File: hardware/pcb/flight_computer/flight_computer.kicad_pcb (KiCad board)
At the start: 4 copper layers, 64 x 64 mm, 96 parts, among them J1 NRF24L01, J2 BATT_TERMINAL, J3 5V Terminal, J4 Pyro 1, J5 Pyro 2, J6 Servo, J7 Servo, J8 Conn_01x02, J9 Aux Ports, Q1 AO3401A, Q2 AO3401A, Q3 2N7002, Q4 AO3400A, Q5 2N7002, Q6 AO3401A, Q7 AO3400A, U2 TPS563201DDCR, U3 TPS73633DRBR, U4 BMP388, U5 LSM6DSRXTR, U6 Teensy4.1, U7 AZ1117-5.0

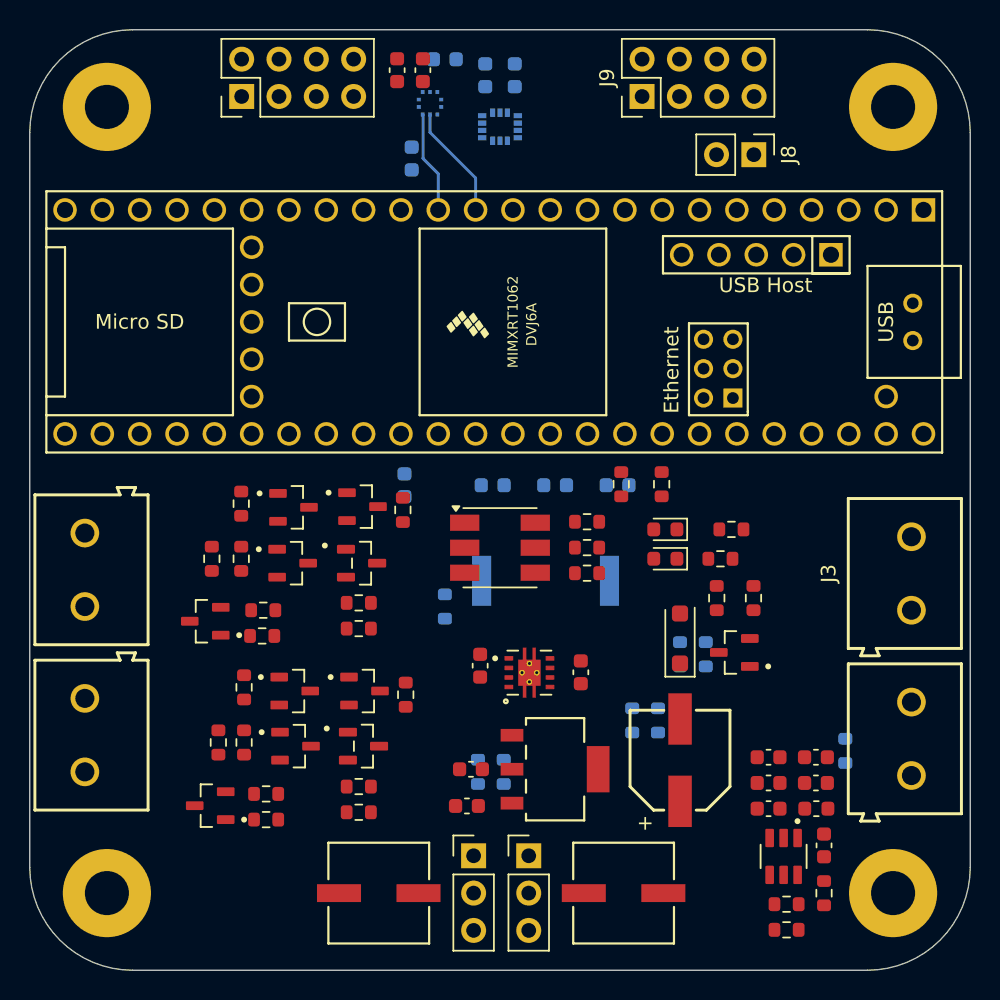
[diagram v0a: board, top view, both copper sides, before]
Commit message: Consolidate simulation and hardware into single ember repo
Absorb the standalone simulation repo into ember as plain files,
add root .gitignore, and update hardware CAD assets.

Co-Authored-By: Claude Opus 4.8 <noreply@anthropic.com>
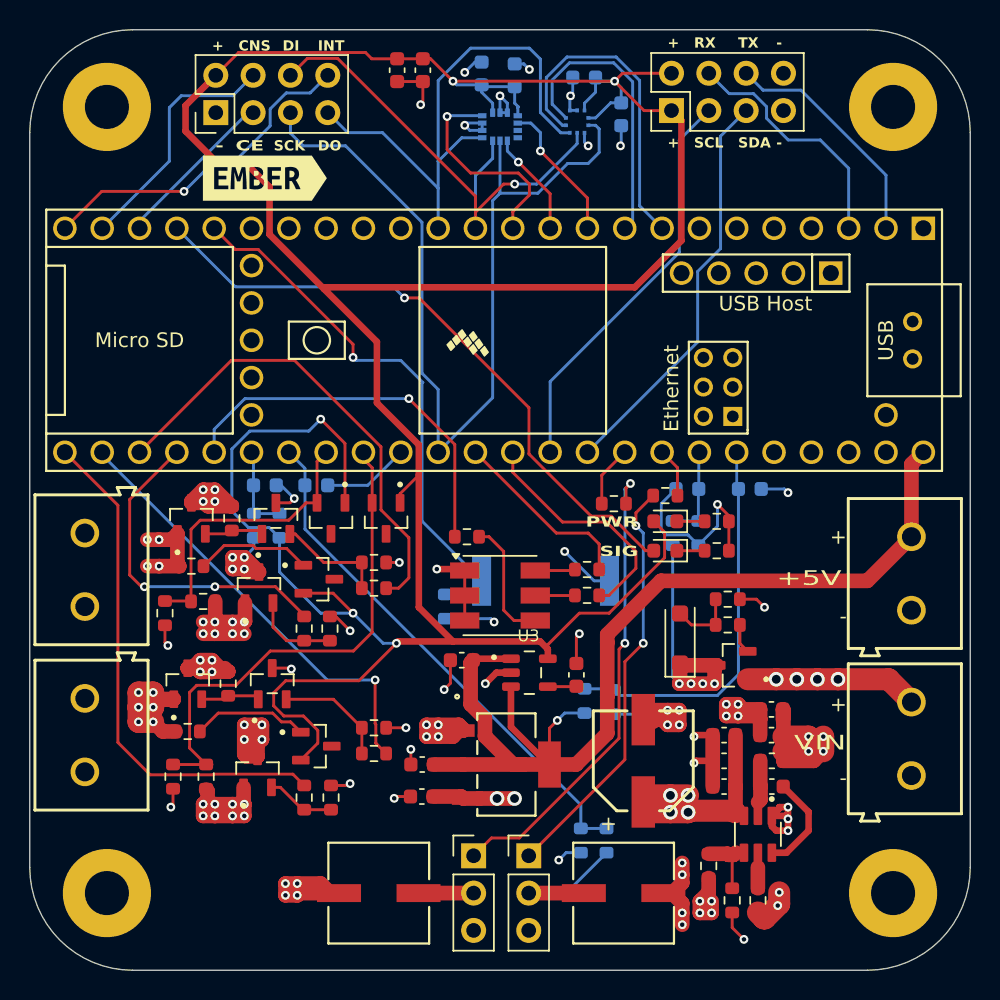
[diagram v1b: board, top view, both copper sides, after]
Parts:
- removed J8: Conn_01x02, Connector_PinHeader_2.54mm:PinHeader_1x02_P2.54mm_Vertical
- added kibuzzard-6A2E09AC: G***, kibuzzard-6A2E09AC, F.Cu at (134.0, 65.6)
- U3: footprint footprints:IC_DRV8601DRBT -> footprints:SOT95P280X145-5N
- moved R18 30.3 mm to (135.0, 89.2)
- moved R19 30.3 mm to (133.2, 89.2)
- moved C19 24.0 mm to (134.0, 86.5)
- moved D3 22.9 mm to (142.2, 88.8), turned to -90 degrees
- moved R17 16.1 mm to (157.8, 101.2)
- moved C4 14.6 mm to (158.2, 61.2)
- moved R7 13.5 mm to (163.5, 89.8)
- moved C12 13.3 mm to (162.8, 86.8)
- moved C18 13.3 mm to (167.0, 86.8)
- moved R6 12.8 mm to (161.8, 89.8)
- moved R8 12.1 mm to (131.5, 100.0), turned to -90 degrees
- moved Q2 12.0 mm to (128.8, 100.0), turned to 90 degrees
- moved Q6 11.7 mm to (129.0, 88.8), turned to 90 degrees
- moved R23 11.7 mm to (131.8, 88.8)
- moved D5 11.1 mm to (138.5, 88.8), turned to -90 degrees
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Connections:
- J1 pad 2: /CE_NRF -> +3.3V
- J1 pad 3: /Barometer/SCK -> /CE_NRF
- J1 pad 4: /Barometer/SDO -> /CNS_NRF
- J1 pad 5: /INT_NRF -> /Barometer/SCK
- J1 pad 7: /CNS_NRF -> /Barometer/SDO
- J1 pad 8: +3.3V -> /INT_NRF
- J4 pad 1: /Pyro 1/PYRO- -> /Pyro 1/PYRO+
- J4 pad 2: /Pyro 1/PYRO+ -> /Pyro 1/PYRO-
- J5 pad 1: /Pyro 2/PYRO- -> /Pyro 2/PYRO+
- J5 pad 2: /Pyro 2/PYRO+ -> /Pyro 2/PYRO-
- J9 pad 3: /SDA -> /SCL
- J9 pad 5: /SCL -> /SDA
- U3 pad 1: +3.3V -> +5V
- U3 pad 2: (no net) -> GND
- U3 pad 3: Net-(U3-NR/FB) -> +5V
- U3 pad 4: GND -> Net-(U3-NR/FB)
- U3 pad 5: +5V -> +3.3V
- U6 pad 10: /CS_IMU -> /INT_IMU_2
- U6 pad 11: /INT_IMU_2 -> /CS_IMU
- U6 pad 22: /CNS_NRF -> /CE_NRF
- U6 pad 23: /CE_NRF -> /CNS_NRF
- U6 pad 25: /Indication/B -> /FIRE_1
- U6 pad 28: /FIRE_1 -> /FIRE_2
- U6 pad 29: /FIRE_2 -> /Indication/B
- U6 pad 32: /CONT_1 -> /CONT_2
- U6 pad 33: /CONT_2 -> /CONT_1
- U6 pad 4: /GPIO_2 -> unconnected-(U6-2_OUT2-Pad4)
- U6 pad 5: /GPIO_1 -> unconnected-(U6-3_LRCLK2-Pad5)
- U7 pad 4: (no net) -> +5V
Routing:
- net +3.3V: track 0.00 -> 219.5 mm, vias 0 -> 5
- net GND: track 0.00 -> 144.6 mm, vias 0 -> 62
- net +5V: track 0.00 -> 72.5 mm, vias 0 -> 1
- net /Barometer/SCK: track 0.00 -> 62.2 mm
- net /Power/VIN: track 0.00 -> 57.4 mm, vias 0 -> 20
- net /Indication/SIGNAL: track 0.00 -> 43.4 mm, vias 0 -> 1
- net /MCU/BUZZER: track 0.00 -> 37.2 mm, vias 0 -> 1
- net /MCU/VDIV_6V: track 0.00 -> 35.6 mm
- net /FIRE_1: track 0.00 -> 35.2 mm
- net /CONT_1: track 0.00 -> 34.6 mm
- net /ARM_2: track 0.00 -> 33.0 mm
- net Net-(J6-Pin_1): track 0.00 -> 32.5 mm, vias 0 -> 2
- net /Barometer/SDO: track 6.94 -> 37.7 mm
- net +6V: track 0.00 -> 30.8 mm, vias 0 -> 8
- net /ARM_1: track 0.00 -> 30.4 mm, vias 0 -> 1
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- added copper zone on In2.Cu, net +6V
- added copper zone on In2.Cu, net /Power/VIN
- added copper zone on In2.Cu, net /Pyro 1/PYRO+
- added copper zone on In2.Cu, net /Pyro 1/PYRO-
- added copper zone on In2.Cu, net /Pyro 2/PYRO+
- added copper zone on In2.Cu, net /Pyro 2/PYRO-
- added copper zone on In2.Cu, net /Reverse Polarity/BAT+
- added copper zone on In1.Cu, net GND
- added copper zone on In2.Cu, net GND
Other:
- board text added: "+"
- board text added: "+5V"
- board text added: "-"
- board text added: "CE"
- board text added: "CNS"
- board text added: "DI"
- board text added: "DO"
- board text added: "INT"
- board text added: "PWR"
- board text added: "RX"
- board text added: "S1"
- board text added: "S2"
- board text added: "SCK"
- board text added: "SCL"
- board text added: "SDA"
- board text added: "SIG"
- board text added: "TX"
- board text added: "VIN"
